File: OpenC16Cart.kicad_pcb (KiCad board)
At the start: 2 copper layers, 50 x 65 mm, 12 parts, among them J1 CONN_01X03, J2 CONN_01X03, J3 CONN_01X03, J4 CONN_01X03, J5 CONN_01X03, J6 CONN_01X03, J7 C16-Exp-Port, U1 27128, U2 27128

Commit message: V2 is almost ready!
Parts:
- removed G***: LOGO, w_logo:Logo_copper_OSHW_6x6mm
- removed J1, J4: CONN_01X03, Pin_Headers:Pin_Header_Straight_1x03
- added A14: CONN_01X03, Pin_Headers:Pin_Header_Straight_1x03, F.Cu at (142.0, 67.1)
- added A14: CONN_01X03, Pin_Headers:Pin_Header_Straight_1x03, F.Cu at (164.8, 67.1)
- added A15: CONN_01X03, Pin_Headers:Pin_Header_Straight_1x03, F.Cu at (145.5, 67.1)
- added A15: CONN_01X03, Pin_Headers:Pin_Header_Straight_1x03, F.Cu at (168.4, 67.1)
- added J1/A13: CONN_02X03, Pin_Headers:Pin_Header_Straight_2x03, F.Cu at (128.8, 67.1)
- added J4/A13: CONN_02X03, Pin_Headers:Pin_Header_Straight_2x03, F.Cu at (151.6, 67.1)
- U1: value 27128 -> LO ROM
- U2: value 27128 -> HI ROM
- moved J3 3.05 mm to (138.4, 67.1)
- moved J6 3.05 mm to (161.3, 67.1)
- moved J2 2.29 mm to (134.9, 67.1)
- moved J5 2.29 mm to (157.7, 67.1)
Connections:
- U1 pad 1: VCC -> /a15_u1
- U1 pad 27: VCC -> /a14_u1
- U2 pad 1: VCC -> /a15_u2
- U2 pad 27: VCC -> /a14_u2
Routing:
- net /a14_u2: track 0.00 -> 65.3 mm
- net /a14_u1: track 0.00 -> 49.9 mm, vias 0 -> 1
- net /a15_u1: track 0.00 -> 48.8 mm
- net /a15_u2: track 0.00 -> 44.3 mm
- net VCC: track 135.5 -> 150.9 mm, vias 0 -> 1
- net GND: track 132.1 -> 144.0 mm
- net /a13_u2: track 41.4 -> 48.3 mm
- net /a12: track 132.5 -> 138.6 mm
- net /a13_u1: track 38.5 -> 44.1 mm
- net /a11_u1: track 43.4 -> 48.9 mm
- net /a11_conn: track 102.6 -> 98.1 mm, vias 0 -> 1
- net /a11_u2: track 38.4 -> 41.0 mm
- net /a13_conn: track 86.2 -> 83.7 mm, vias 0 -> 1
- net Net-(J7-PadB): track 31.0 -> 32.9 mm
- net /a2: track 64.8 -> 66.5 mm
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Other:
- outline, holes or cut-outs redrawn
- board text added: "HI"
- board text added: "LO"
- board text added: "V2"
- board text added: "github.com/SukkoPera/OpenC16Cart"
- board text removed: "V1.0"
- board text removed: "https://github.com/SukkoPera/OpenC16Cart"

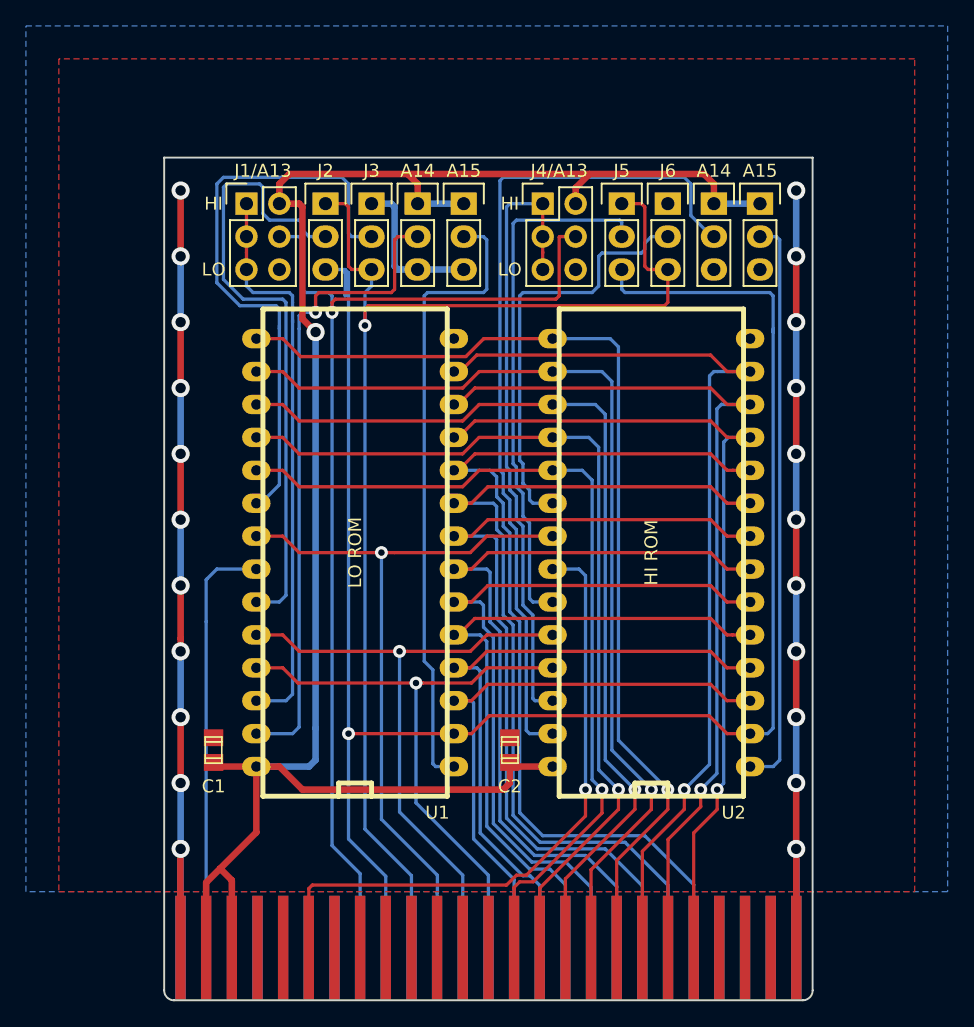
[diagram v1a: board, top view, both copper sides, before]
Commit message: Make board slightly larger
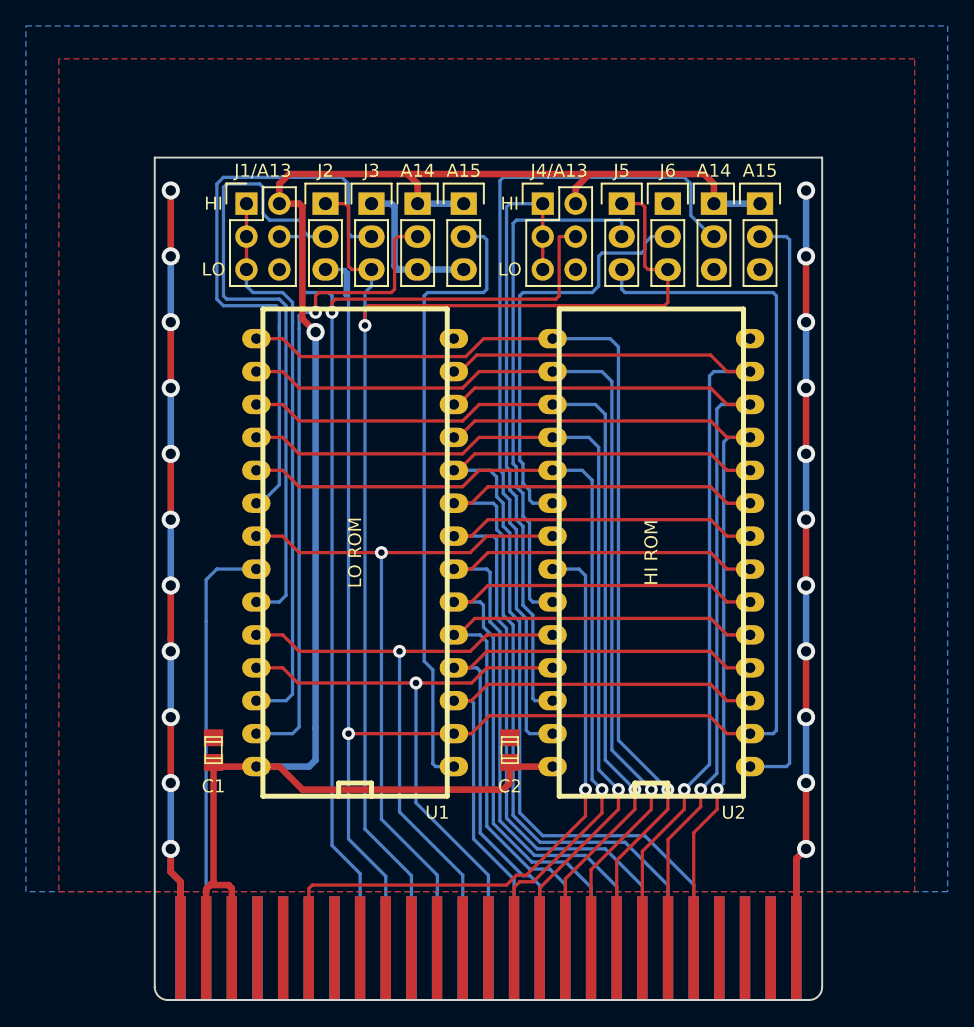
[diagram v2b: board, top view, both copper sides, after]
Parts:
- J7: footprint Sukko:C16_Cart_Conn -> C16_Cart_Conn:C16_Cart_Conn
- moved J7 3.96 mm to (147.4, 124.5)
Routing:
- net /a15_u2: track 44.3 -> 45.9 mm
- net GND: track 144.0 -> 145.4 mm
- net VCC: track 150.9 -> 149.7 mm
- net //ce_u1: track 45.7 -> 46.5 mm
- net /a11_u1: track 48.9 -> 49.5 mm
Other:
- board size 50 x 65 mm -> 51.5 x 65 mm

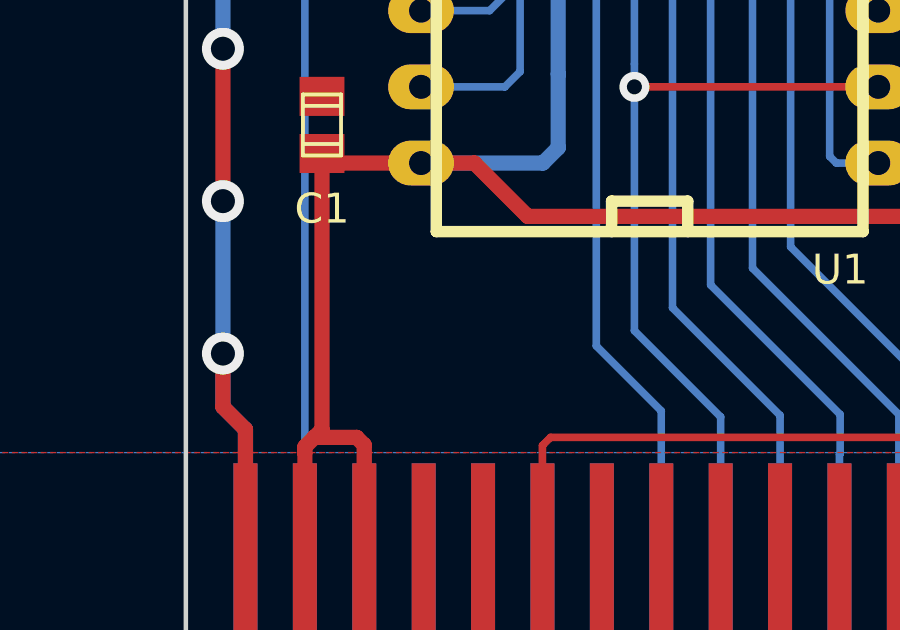
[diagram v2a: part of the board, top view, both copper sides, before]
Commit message: Add OSHW logo
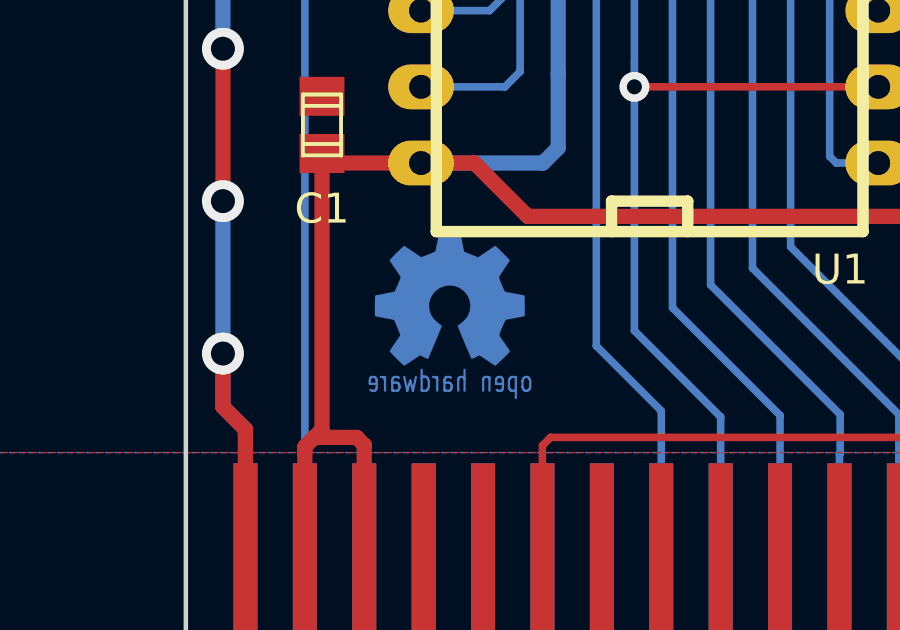
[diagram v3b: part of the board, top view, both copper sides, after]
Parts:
- added G***: LOGO, w_logo:Logo_copper_OSHW_6x6mm, B.Cu at (130.5, 115.0)

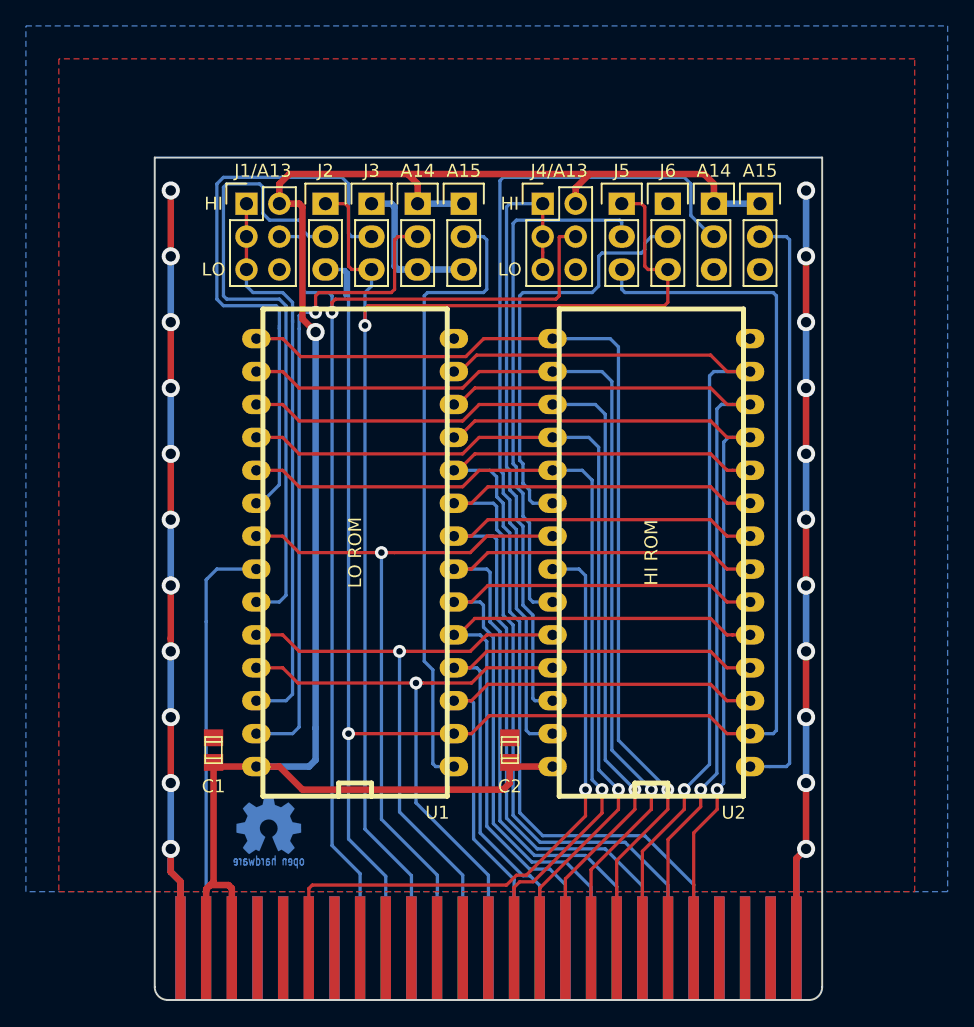
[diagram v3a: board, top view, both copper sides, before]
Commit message: Switch to C_0805_HandSoldering and rebuild whatever is needed
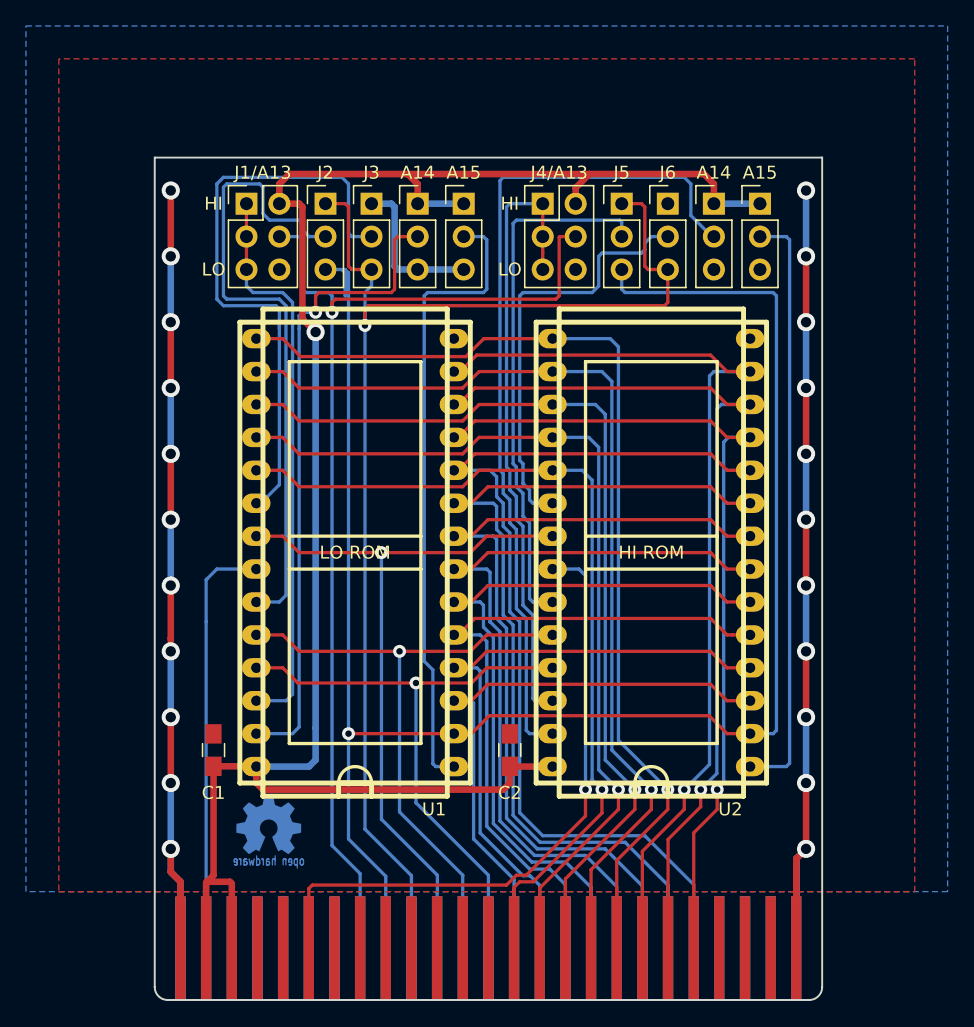
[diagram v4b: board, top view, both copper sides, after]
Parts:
- removed A14 (x2), A15 (x2): CONN_01X03, Pin_Headers:Pin_Header_Straight_1x03
- removed J1/A13, J4/A13: CONN_02X03, Pin_Headers:Pin_Header_Straight_2x03
- added J1: CONN_02X03, Pin_Headers:Pin_Header_Straight_2x03_Pitch2.54mm, F.Cu at (128.8, 67.1)
- added J11: CONN_01X03, Pin_Headers:Pin_Header_Straight_1x03_Pitch2.54mm, F.Cu at (142.0, 67.1)
- added J12: CONN_01X03, Pin_Headers:Pin_Header_Straight_1x03_Pitch2.54mm, F.Cu at (145.5, 67.1)
- added J21: CONN_01X03, Pin_Headers:Pin_Header_Straight_1x03_Pitch2.54mm, F.Cu at (164.8, 67.1)
- added J22: CONN_01X03, Pin_Headers:Pin_Header_Straight_1x03_Pitch2.54mm, F.Cu at (168.4, 67.1)
- added J4: CONN_02X03, Pin_Headers:Pin_Header_Straight_2x03_Pitch2.54mm, F.Cu at (151.6, 67.1)
- C1, C2: footprint smd_cap:c_0805 -> Capacitors_SMD:C_0805_HandSoldering
- J2, J3, J5, J6: footprint Pin_Headers:Pin_Header_Straight_1x03 -> Pin_Headers:Pin_Header_Straight_1x03_Pitch2.54mm
- U1: value LO ROM -> 27512 - LO ROM; footprint pth_circuits:dil_28-600 -> w_pth_circuits:dil_28-600_socket
- U2: value HI ROM -> 27512 - HI ROM; footprint pth_circuits:dil_28-600 -> w_pth_circuits:dil_28-600_socket
- turned C1 to 270 degrees
- turned C2 to 270 degrees
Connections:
- J7 pad 10: (no net) -> Net-(J7-Pad10)
- J7 pad 11: (no net) -> Net-(J7-Pad11)
- J7 pad 12: (no net) -> Net-(J7-Pad12)
- J7 pad 13: (no net) -> Net-(J7-Pad13)
- J7 pad 22: (no net) -> Net-(J7-Pad22)
- J7 pad 23: (no net) -> Net-(J7-Pad23)
- J7 pad 24: (no net) -> Net-(J7-Pad24)
- J7 pad 4: (no net) -> Net-(J7-Pad4)
- J7 pad 5: (no net) -> Net-(J7-Pad5)
- J7 pad 7: (no net) -> Net-(J7-Pad7)
- J7 pad 8: (no net) -> Net-(J7-Pad8)
- J7 pad 9: (no net) -> Net-(J7-Pad9)
- J7 pad AA: (no net) -> Net-(J7-PadAA)
- J7 pad BB: (no net) -> Net-(J7-PadBB)
- J7 pad C: (no net) -> Net-(J7-PadC)
- J7 pad D: (no net) -> Net-(J7-PadD)
- J7 pad E: (no net) -> Net-(J7-PadE)
- J7 pad F: (no net) -> Net-(J7-PadF)
- J7 pad H: (no net) -> Net-(J7-PadH)
- J7 pad Z: (no net) -> Net-(J7-PadZ)
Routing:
- net VCC: track 149.7 -> 150.8 mm
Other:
- net class Default: clearance 0.254 -> 0.25
- rule trace_clearance: 0.254 -> 0.25
- board text added: "A14"
- board text added: "A15"
- board text added: "HI ROM"
- board text added: "J1/A13"
- board text added: "J4/A13"
- board text added: "LO ROM"

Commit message: Space edge connector pins 2.0mm apart
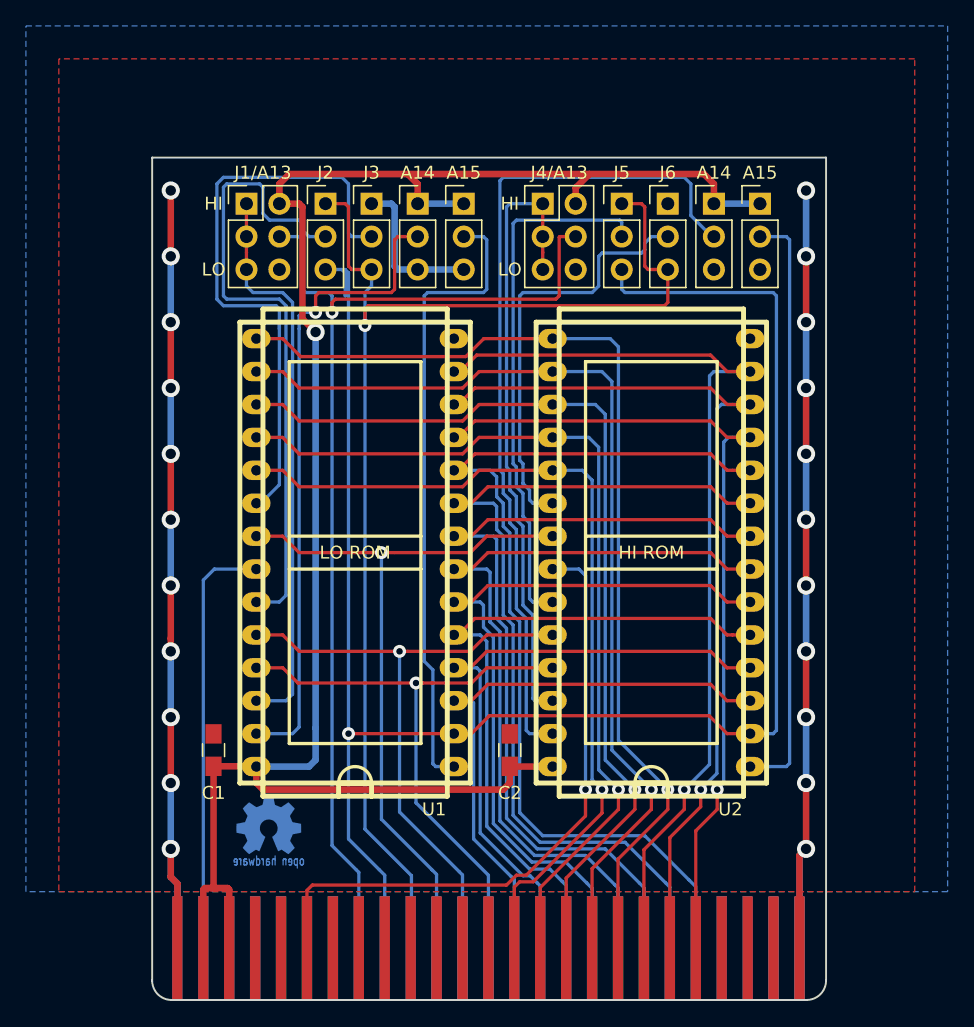
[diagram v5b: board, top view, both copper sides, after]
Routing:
- net VCC: track 150.8 -> 150.2 mm
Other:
- board size 51.5 x 65 mm -> 52 x 65 mm

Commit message: Tighter soldermask
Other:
- rule pad_to_mask_clearance: 0.2 -> 0
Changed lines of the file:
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@@
   (layers
     (0 F.Cu signal)
-    (31 B.Cu signal hide)
-    (36 B.SilkS user hide)
+    (31 B.Cu signal)
+    (36 B.SilkS user)
     (37 F.SilkS user)
-    (38 B.Mask user hide)
-    (39 F.Mask user hide)
+    (38 B.Mask user)
+    (39 F.Mask user)
     (44 Edge.Cuts user)
     (47 F.CrtYd user hide)
@@
     (pad_size 1.524 1.524)
     (pad_drill 0.762)
-    (pad_to_mask_clearance 0.2)
+    (pad_to_mask_clearance 0)
     (aux_axis_origin 0 0)
     (grid_origin 121.5 128.5)
@@
     (connect_pads (clearance 0.125))
     (min_thickness 0.0254)
-    (fill yes (arc_segments 16) (thermal_gap 0.508) (thermal_bridge_width 0.508))
+    (fill yes (arc_segments 16) (thermal_gap 0.254) (thermal_bridge_width 0.508))
     (polygon
       (pts
@@
     (connect_pads (clearance 0.125))
     (min_thickness 0.0254)
-    (fill yes (arc_segments 16) (thermal_gap 0.508) (thermal_bridge_width 0.508))
+    (fill yes (arc_segments 16) (thermal_gap 0.254) (thermal_bridge_width 0.508))
     (polygon
       (pts
